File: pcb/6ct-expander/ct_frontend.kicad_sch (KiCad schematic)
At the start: 9 parts, among them J1 SJ-3524-SMT-TR

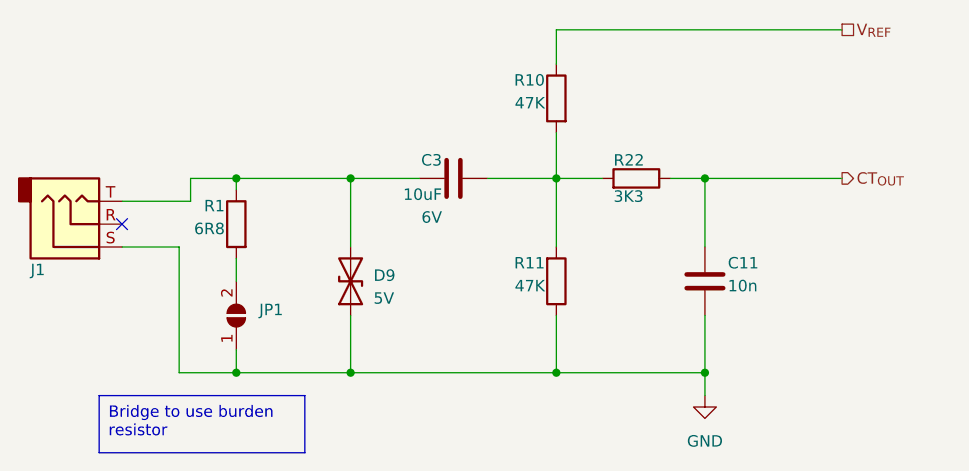
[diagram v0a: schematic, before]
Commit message: [6CT] Finalise CT expander board
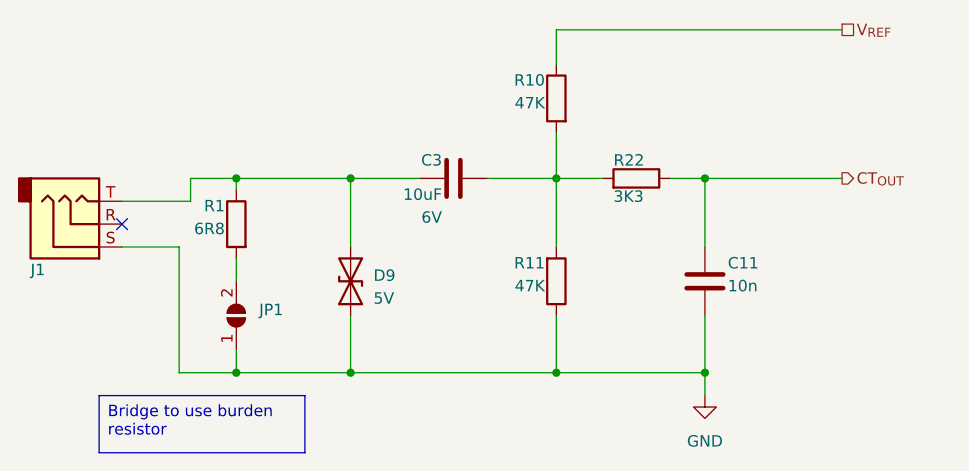
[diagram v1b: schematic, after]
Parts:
- C11: LCSC (none) -> C57112
- C3: LCSC (none) -> C19702
- D9: LCSC (none) -> C1973289
- J1: LCSC (none) -> C20182907
- R1: LCSC (none) -> C25345
- R10, R11: LCSC (none) -> C23162
- R22: LCSC (none) -> C22978

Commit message: Freeze for manufacture
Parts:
- JP1: now not fitted
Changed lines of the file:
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@@
 		(in_bom yes)
 		(on_board yes)
-		(dnp no)
+		(dnp yes)
 		(fields_autoplaced yes)
 		(property "Reference" "JP1"

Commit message: Alternate jack for manufacture
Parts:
- J1: LCSC C20182907 -> C4991872
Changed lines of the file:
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@@
 			)
 		)
-		(property "LCSC" "C20182907"
+		(property "LCSC" "C4991872"
 			(at 97.79 90.17 0)
 			(effects
